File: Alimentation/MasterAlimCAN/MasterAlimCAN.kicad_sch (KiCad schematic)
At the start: 27 parts, among them J1 BATT, J12 Alim I/O, U1 AMS1117-3.3, U2 STM32G474RETx, Y1 16MHz

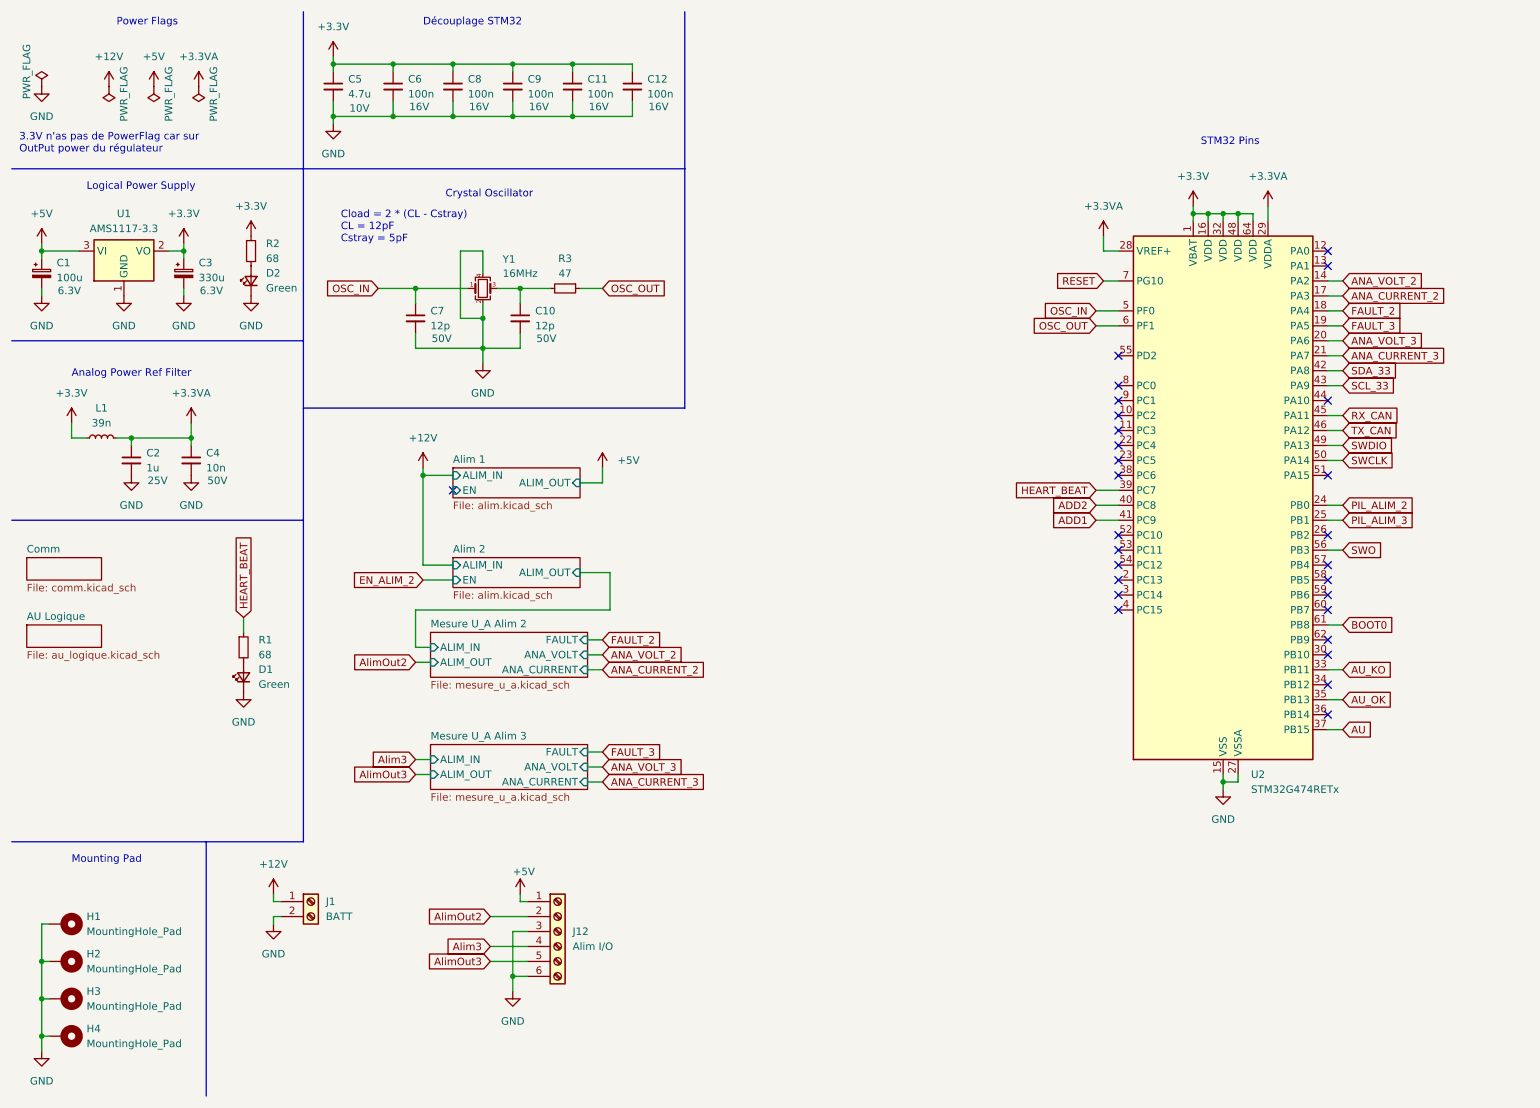
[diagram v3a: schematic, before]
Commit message: New placement for Alim
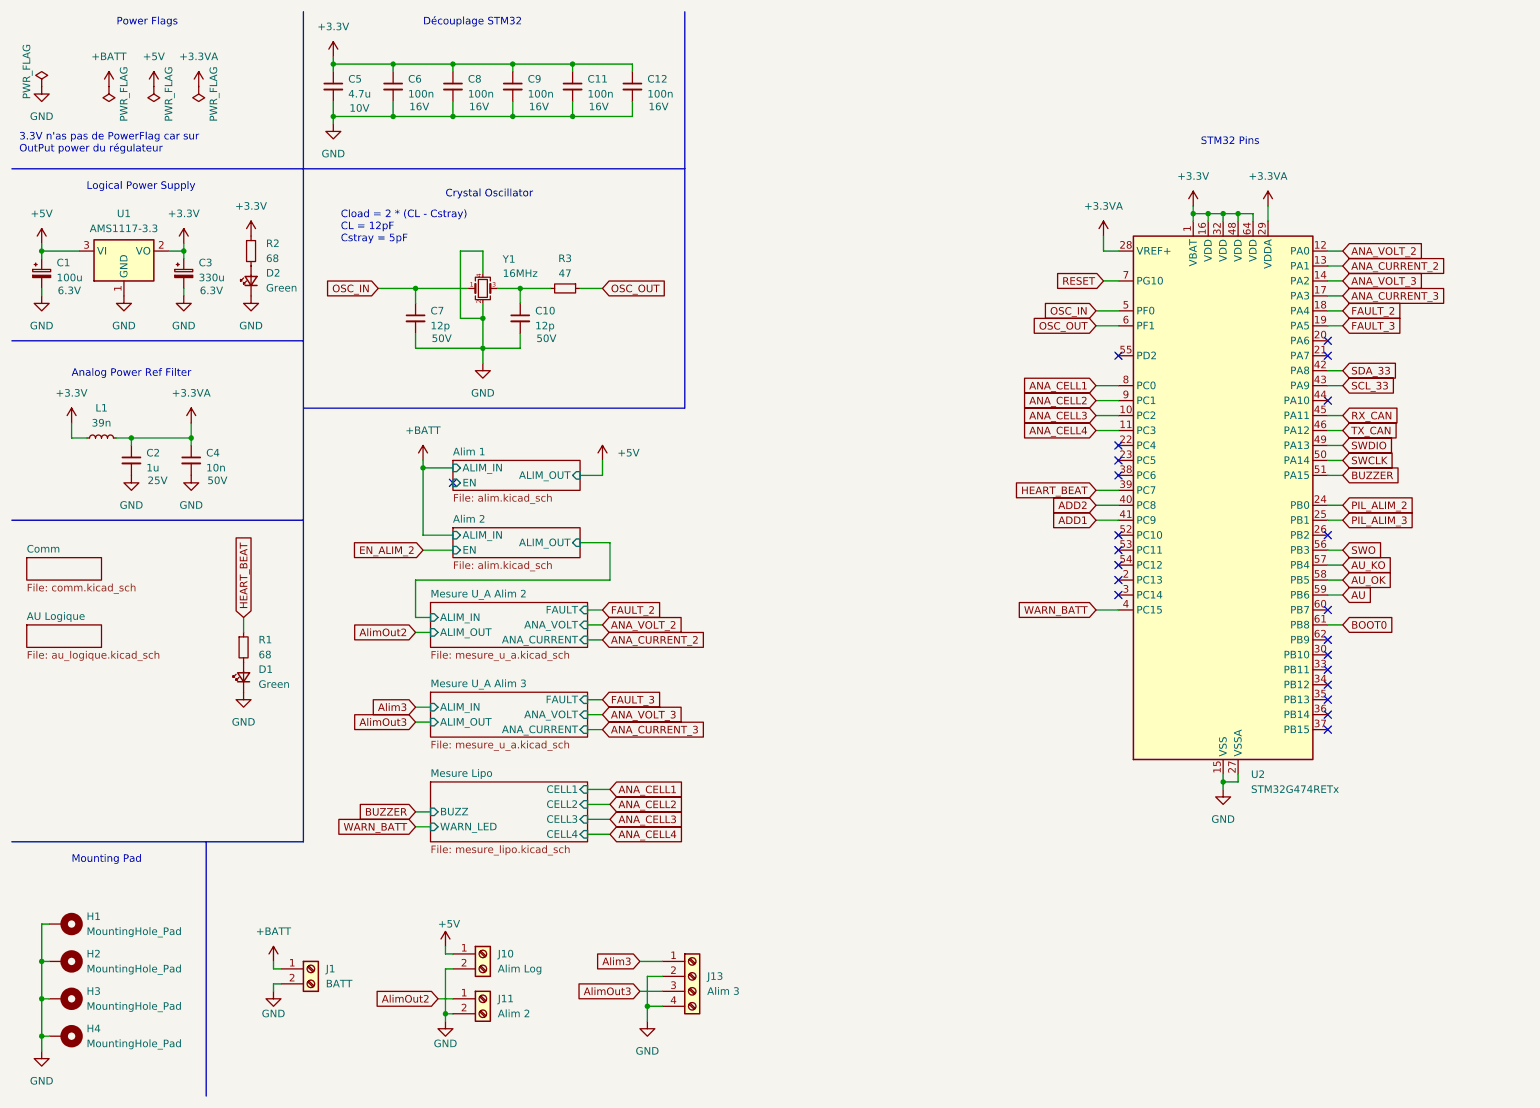
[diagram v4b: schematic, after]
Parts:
- removed J12: Alim I/O, TerminalBlock_Phoenix:TerminalBlock_Phoenix_MKDS-1,5-6-5.08_1x06_P5.08mm_Horizontal, symbol Connector:Screw_Terminal_01x06
- added J10: Alim Log, TerminalBlock_Phoenix:TerminalBlock_Phoenix_MKDS-1,5-2-5.08_1x02_P5.08mm_Horizontal, symbol Connector:Screw_Terminal_01x02
- added J11: Alim 2, TerminalBlock_Phoenix:TerminalBlock_Phoenix_MKDS-1,5-2-5.08_1x02_P5.08mm_Horizontal, symbol Connector:Screw_Terminal_01x02
- added J13: Alim 3, TerminalBlock_Phoenix:TerminalBlock_Phoenix_MKDS-1,5-4-5.08_1x04_P5.08mm_Horizontal, symbol Connector:Screw_Terminal_01x04
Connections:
- net +5V: now also J10.1 (Pin_1)
- net ANA_CURRENT_2: now also U2.13 (PA1); no longer U2.17 (PA3)
- net ANA_CURRENT_3: now also U2.17 (PA3); no longer U2.21 (PA7)
- net ANA_VOLT_2: now also U2.12 (PA0); no longer U2.14 (PA2)
- net ANA_VOLT_3: now also U2.14 (PA2); no longer U2.20 (PA6)
- net AU: now also U2.59 (PB6); no longer U2.37 (PB15)
- net AU_KO: now also U2.57 (PB4); no longer U2.33 (PB11)
- net AU_OK: now also U2.58 (PB5); no longer U2.35 (PB13)
- net Alim3: now also J13.1 (Pin_1)
- net AlimOut2: now also J11.1 (Pin_1)
- net AlimOut3: now also J13.3 (Pin_3)
- net GND: now also J10.2 (Pin_2), J11.2 (Pin_2), J13.2 (Pin_2), J13.4 (Pin_4)
- net ANA_CELL3: now reaches U2.10 (PC2)
- net ANA_CELL4: now reaches U2.11 (PC3)
- net WARN_BATT: now reaches U2.4 (PC15)
- net BUZZER: now reaches U2.51 (PA15)
- net ANA_CELL1: now reaches U2.8 (PC0)
- net ANA_CELL2: now reaches U2.9 (PC1)
- net +12V renamed +BATT
- no-connect marks 28 -> 22
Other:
- added sheet Mesure Lipo (mesure_lipo.kicad_sch)
- moved on the sheet: J1

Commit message: Finish component placement on MasterAlimCAN
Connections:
- net ANA_CELL1: now also U2.11 (PC3); no longer U2.8 (PC0)
- net ANA_CELL2: now also U2.10 (PC2); no longer U2.9 (PC1)
- net ANA_CELL3: now also U2.9 (PC1); no longer U2.10 (PC2)
- net ANA_CELL4: now also U2.8 (PC0); no longer U2.11 (PC3)

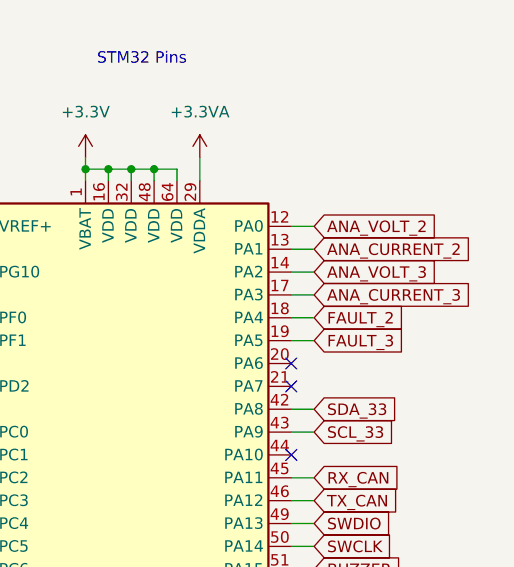
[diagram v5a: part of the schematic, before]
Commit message: Upgrade to KiCad 8 and finish routing
- MasterAlimCAN
- InterfaceRaspiCAN
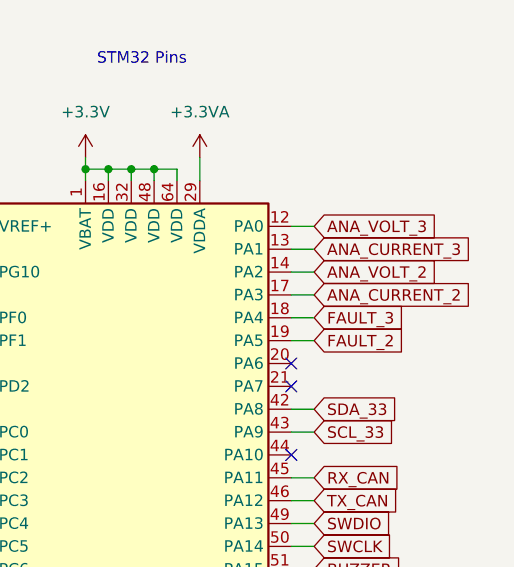
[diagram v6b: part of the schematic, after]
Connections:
- net ANA_CURRENT_2: now also U2.17 (PA3); no longer U2.13 (PA1)
- net ANA_CURRENT_3: now also U2.13 (PA1); no longer U2.17 (PA3)
- net ANA_VOLT_2: now also U2.14 (PA2); no longer U2.12 (PA0)
- net ANA_VOLT_3: now also U2.12 (PA0); no longer U2.14 (PA2)
- net FAULT_2: now also U2.19 (PA5); no longer U2.18 (PA4)
- net FAULT_3: now also U2.18 (PA4); no longer U2.19 (PA5)
